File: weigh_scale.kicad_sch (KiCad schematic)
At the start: 13 parts, among them J1 Conn_01x04_Pin, SW1 SW_Push, SW2 SW_Push, U1 HX711, U2 ATtiny85-20S

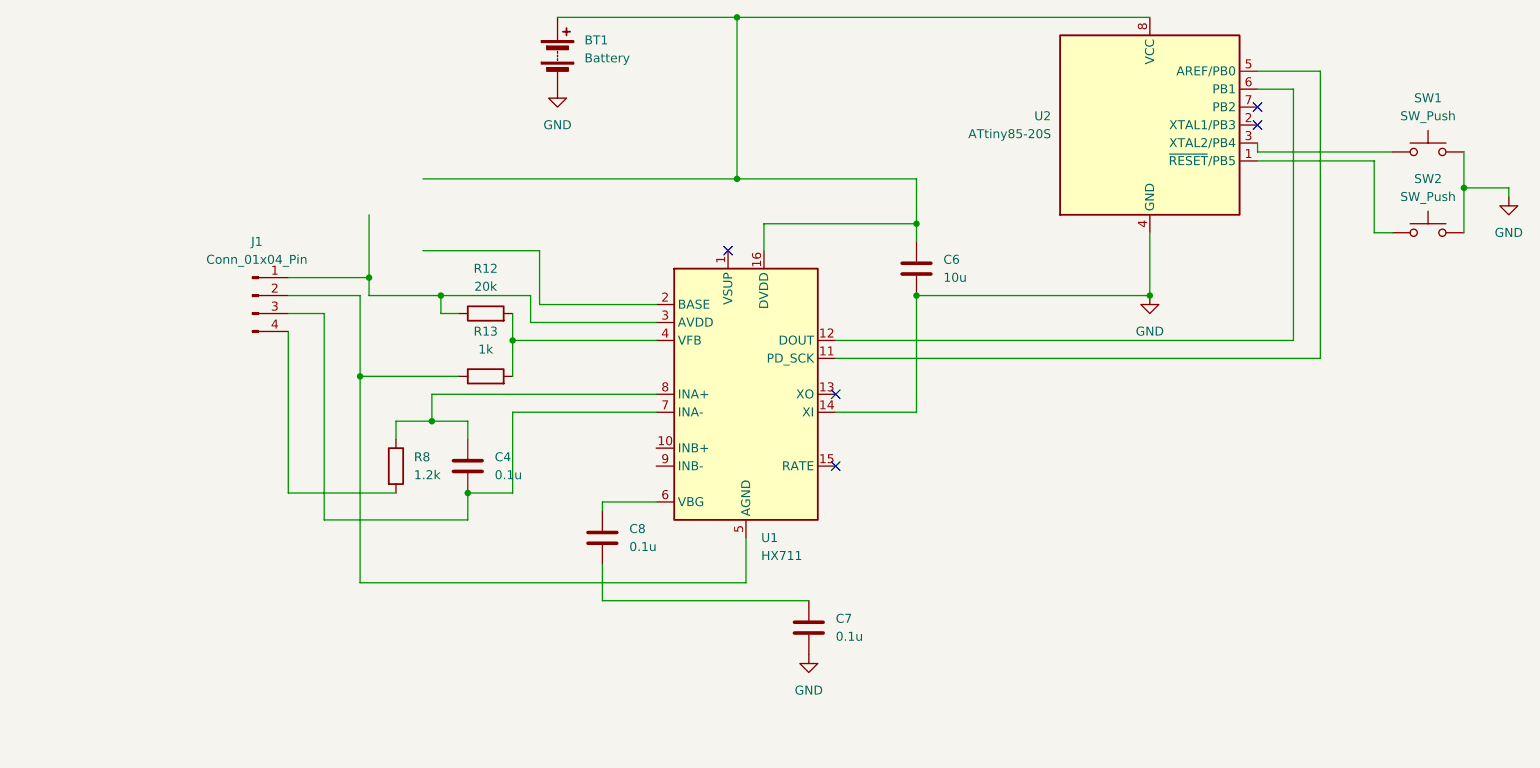
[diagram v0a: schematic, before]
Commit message: Updated schematic for Xiao esp32c3
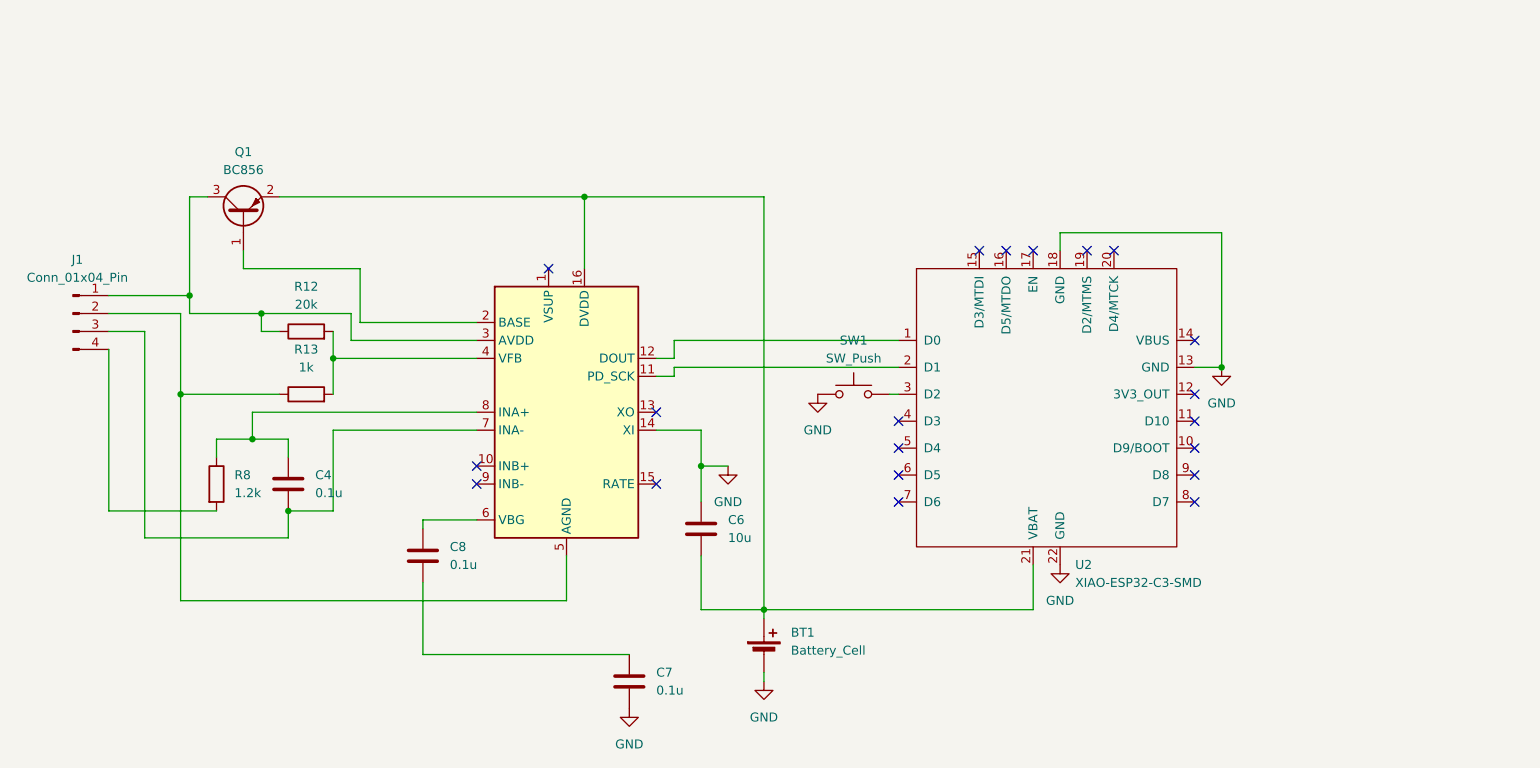
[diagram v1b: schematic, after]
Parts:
- removed BT1: Battery, symbol Device:Battery
- removed SW2: SW_Push, symbol Switch:SW_Push
- removed U2: ATtiny85-20S, Package_SO:SOIC-8_5.3x5.3mm_P1.27mm, symbol MCU_Microchip_ATtiny:ATtiny85-20S
- added BT1: Battery_Cell, Battery:BatteryHolder_Keystone_1042_1x18650, symbol Device:Battery_Cell
- added Q1: BC856, Package_TO_SOT_SMD:SOT-23, symbol Transistor_BJT:BC856
- added U2: XIAO-ESP32-C3-SMD, RF_Module:MCU_Seeed_ESP32C3, symbol Seeed_Studio_XIAO_Series:XIAO-ESP32-C3-SMD
- C4, C6, C7, C8: footprint (none) -> Capacitor_SMD:C_0805_2012Metric_Pad1.18x1.45mm_HandSolder
- J1: footprint (none) -> Connector_Wire:SolderWire-0.5sqmm_1x04_P4.8mm_D0.9mm_OD2.3mm
- R12, R13, R8: footprint (none) -> Resistor_SMD:R_0805_2012Metric_Pad1.20x1.40mm_HandSolder
- SW1: footprint (none) -> Button_Switch_THT:SW_Slide_SPDT_Straight_CK_OS102011MS2Q
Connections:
- net GND: now also C6.1, SW1.1, BT1.2 (-), U2.13 (GND), U2.18 (GND), U2.22 (GND); no longer C6.2, SW1.2
- net at J1.1 (Pin_1), R12.1, U1.3 (AVDD): now also Q1.3 (C)
- net at U1.11 (PD_SCK): now also U2.2 (D1)
- net at U1.12 (DOUT): now also U2.1 (D0)
- net at U1.16 (DVDD): now also C6.2, BT1.1 (+), Q1.2 (E), U2.21 (VBAT); no longer C6.1
- net at U1.2 (BASE): now also Q1.1 (B)
- new net: SW1.2, U2.3 (D2)
- no-connect marks 5 -> 20
